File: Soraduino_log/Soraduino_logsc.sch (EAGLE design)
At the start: 26 parts, among them IC1 ATMEGA168-AU, IC2 LM1117IMPX-3.3, IC3 LM1117MPX-5.0

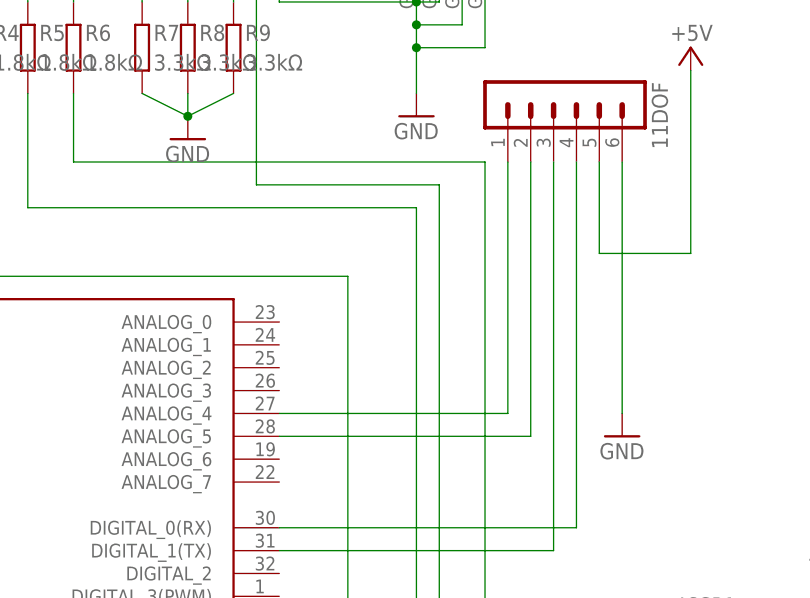
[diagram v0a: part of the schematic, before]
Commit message: fix I2C port mistake about sch
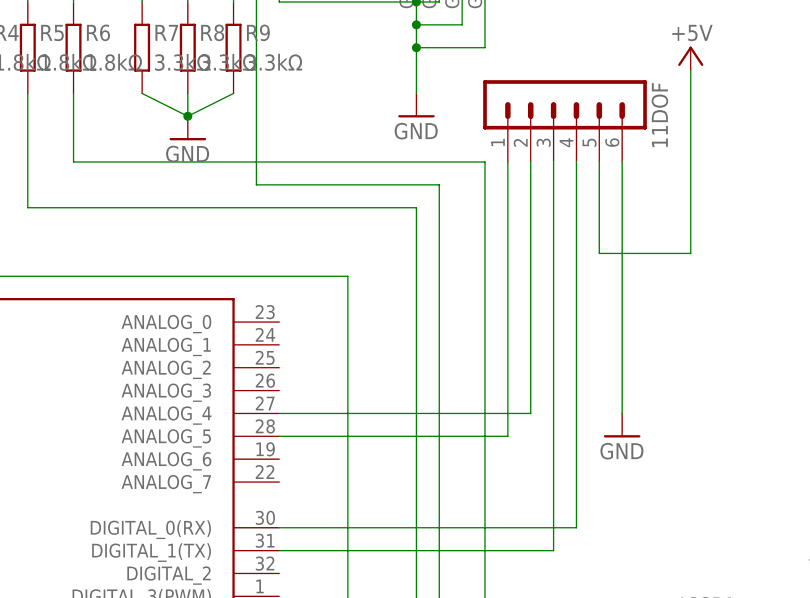
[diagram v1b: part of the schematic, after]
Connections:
- removed net N$9: 11DOF.2, IC1.ANALOG_5
- new net N$3: 11DOF.1, IC1.ANALOG_5
- net N$8: now also 11DOF.2; no longer 11DOF.1
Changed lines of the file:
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@@
 <?xml version="1.0" encoding="utf-8"?>
 <!DOCTYPE eagle SYSTEM "eagle.dtd">
-<eagle version="6.4">
+<eagle version="6.5.0">
 <drawing>
 <settings>
@@
 <segment>
 <pinref part="IC1" gate="1" pin="ANALOG_4"/>
-<pinref part="11DOF" gate="1" pin="1"/>
-<wire x1="91.44" y1="71.12" x2="116.84" y2="71.12" width="0.1524" layer="91"/>
-<wire x1="116.84" y1="71.12" x2="116.84" y2="99.06" width="0.1524" layer="91"/>
-</segment>
-</net>
-<net name="N$9" class="0">
-<segment>
-<pinref part="IC1" gate="1" pin="ANALOG_5"/>
+<wire x1="91.44" y1="71.12" x2="119.38" y2="71.12" width="0.1524" layer="91"/>
 <pinref part="11DOF" gate="1" pin="2"/>
-<wire x1="91.44" y1="68.58" x2="119.38" y2="68.58" width="0.1524" layer="91"/>
-<wire x1="119.38" y1="68.58" x2="119.38" y2="99.06" width="0.1524" layer="91"/>
+<wire x1="119.38" y1="71.12" x2="119.38" y2="99.06" width="0.1524" layer="91"/>
 </segment>
 </net>
@@
 </segment>
 </net>
+<net name="N$3" class="0">
+<segment>
+<pinref part="IC1" gate="1" pin="ANALOG_5"/>
+<pinref part="11DOF" gate="1" pin="1"/>
+<wire x1="91.44" y1="68.58" x2="116.84" y2="68.58" width="0.1524" layer="91"/>
+<wire x1="116.84" y1="68.58" x2="116.84" y2="99.06" width="0.1524" layer="91"/>
+</segment>
+</net>
 </nets>
 </sheet>
 </sheets>
-<errors>
-</errors>
 </schematic>
 </drawing>
